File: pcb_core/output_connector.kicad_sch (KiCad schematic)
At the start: 5 parts, among them IC1 DRV8871DDA, J3 1053131103

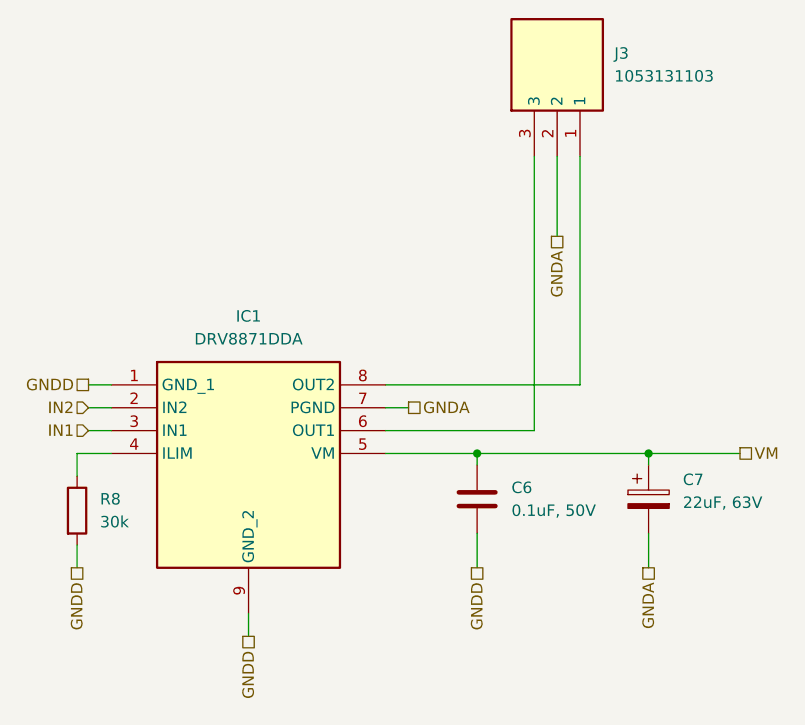
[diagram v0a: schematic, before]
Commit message: Correct BOM errors
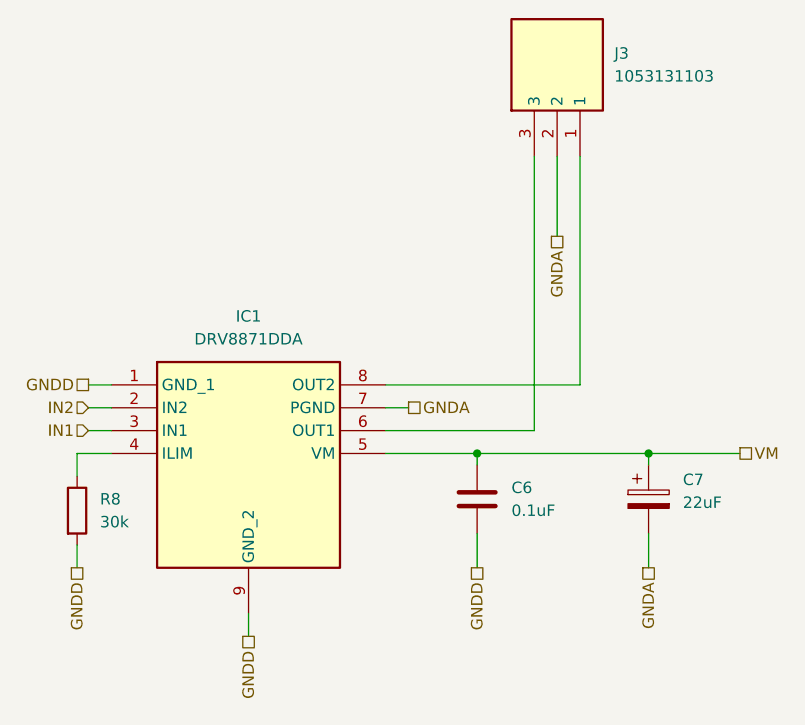
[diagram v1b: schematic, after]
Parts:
- C6: value 0.1uF, 50V -> 0.1uF
- C7: value 22uF, 63V -> 22uF
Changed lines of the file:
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@@
 			)
 		)
-		(property "Value" "0.1uF, 50V"
+		(property "Value" "0.1uF"
 			(at 128.27 111.7599 0)
 			(effects
@@
 			)
 		)
-		(property "Value" "22uF, 63V"
+		(property "Value" "22uF"
 			(at 147.32 110.8709 0)
 			(effects

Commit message: Correct ECR Warnings
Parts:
- IC1: Arrow Part Number (none) -> DRV8871DDA; Arrow Price/Stock (none) -> https://www.arrow.com/en/products/drv8871dda/texas-instrume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; Mouser Price/Stock (none) -> https://www.mouser.co.uk/ProductDetail/Texas-Instruments/DR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
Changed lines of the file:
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@@
 			)
 		)
-		(property "Description" ""
+		(property "Description" "Motor / Motion / Ignition Controllers & Drivers 3.6A Brushed DC Motor Driver with Integrated Current Sensing (PWM Ctrl) 8-SO PowerPAD -40 to 125"
 			(at 83.82 97.79 0)
 			(effects
@@
 				(hide yes)
 			)
+		)
+		(property "Mouser Price/Stock" "https://www.mouser.co.uk/ProductDetail/Texas-Instruments/DRV8871DDA?qs=Fobv33ltQGiluwfB07aSBw%3D%3D"
+			(at 110.49 892.71 0)
+			(effects
+				(font
+					(size 1.27 1.27)
+				)
+				(justify left top)
+				(hide yes)
+			)
+		)
+		(property "Arrow Part Number" "DRV8871DDA"
+			(at 110.49 992.71 0)
+			(effects
+				(font
+					(size 1.27 1.27)
+				)
+				(justify left top)
+				(hide yes)
+			)
+		)
+		(property "Arrow Price/Stock" "https://www.arrow.com/en/products/drv8871dda/texas-instruments?region=nac"
+			(at 110.49 1092.71 0)
+			(effects
+				(font
+					(size 1.27 1.27)
+				)
+				(justify left top)
+				(hide yes)
+			)

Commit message: Harmonize package sizing of components
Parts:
- C6: Manufacturer_Part_Number (none) -> Capacitor, 0.1uF, 50V, 0805 SMD
- C7: LCSC# C473196 -> C5246567; Manufacturer_Part_Number (none) -> Polarized Capacitor, 22.0uF, 63V, D6.3xL7.7 SMD
- R8: LCSC# C319666 -> C2907479
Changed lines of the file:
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@@
 			)
 		)
-		(property "Manufacturer_Part_Number" ""
+		(property "Manufacturer_Part_Number" "Capacitor, 0.1uF, 50V, 0805 SMD"
 			(at 124.46 110.49 0)
 			(effects
@@
 			)
 		)
-		(property "Manufacturer_Part_Number" ""
+		(property "Manufacturer_Part_Number" "Polarized Capacitor, 22.0uF, 63V, D6.3xL7.7 SMD"
 			(at 143.51 110.49 0)
 			(effects
@@
 			)
 		)
-		(property "LCSC#" "C473196"
+		(property "LCSC#" "C5246567"
 			(at 143.51 110.49 0)
 			(effects
@@
 			)
 		)
-		(property "LCSC#" "C319666"
+		(property "LCSC#" "C2907479"
 			(at 80.01 111.76 0)
 			(effects

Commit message: Add AISLER bom support and assigned components
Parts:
- C6: AISLER_MPN (none) -> 100.0nF, 0805 SMD
- IC1: AISLER_MPN (none) -> DRV8871DDA
- J3: AISLER_MPN (none) -> 1053131103
- R8: AISLER_MPN (none) -> 30.0kΩ, 1206 SMD
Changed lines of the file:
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@@
+			)
+		)
+		(property "AISLER_MPN" "100.0nF, 0805 SMD"
+			(at 124.46 110.49 0)
+			(effects
+				(font
+					(size 1.27 1.27)
+				)
+				(hide yes)
 			)
 		)
@@
 			)
 		)
+		(property "AISLER_MPN" ""
+			(at 143.51 110.49 0)
+			(effects
+				(font
+					(size 1.27 1.27)
+				)
+				(hide yes)
+			)
+		)
 		(pin "1"
 		)
@@
 			)
 		)
+		(property "AISLER_MPN" "DRV8871DDA"
+			(at 83.82 97.79 0)
+			(effects
+				(font
+					(size 1.27 1.27)
+				)
+				(hide yes)
+			)
+		)
 		(pin "9"
 		)
@@
 			)
 		)
+		(property "AISLER_MPN" "30.0kΩ, 1206 SMD "
+			(at 80.01 111.76 0)
+			(effects
+				(font
+					(size 1.27 1.27)
+				)
+				(hide yes)
+			)
+		)
 		(pin "1"
 		)
@@
 			(at 130.81 72.39 0)
 			(effects
+				(font
+					(size 1.27 1.27)
+				)
+				(hide yes)
+			)
+		)
+		(property "AISLER_MPN" "1053131103"
+			(at 130.81 72.39 0)
+			(effects

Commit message: Update BOM Mouser
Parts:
- C6: Mouser Part Number (none) -> 80-C0805C104M5R
- C7: Mouser Part Number (none) -> 710-865080745011
- R8: Mouser Part Number (none) -> 652-CR1206FX-3002ELF
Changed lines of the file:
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@@
+			)
+		)
+		(property "Mouser Part Number" " 80-C0805C104M5R "
+			(at 124.46 110.49 0)
+			(effects
+				(font
+					(size 1.27 1.27)
+				)
+				(hide yes)
+			)
+		)
+		(property "Mouser# Alt1" ""
+			(at 124.46 110.49 0)
+			(effects
+				(font
+					(size 1.27 1.27)
+				)
+				(hide yes)
 			)
 		)
@@
 			)
 		)
+		(property "Mouser Part Number" "710-865080745011"
+			(at 143.51 110.49 0)
+			(effects
+				(font
+					(size 1.27 1.27)
+				)
+				(hide yes)
+			)
+		)
+		(property "Mouser# Alt1" ""
+			(at 143.51 110.49 0)
+			(effects
+				(font
+					(size 1.27 1.27)
+				)
+				(hide yes)
+			)
+		)
 		(pin "1"
 		)
@@
 			)
 		)
+		(property "Mouser# Alt1" ""
+			(at 83.82 97.79 0)
+			(effects
+				(font
+					(size 1.27 1.27)
+				)
+				(hide yes)
+			)
+		)
 		(pin "9"
 		)
@@
 			)
 		)
+		(property "Mouser Part Number" "652-CR1206FX-3002ELF "
+			(at 80.01 111.76 0)
+			(effects
+				(font
+					(size 1.27 1.27)
+				)
+				(hide yes)
+			)
+		)
+		(property "Mouser# Alt1" ""
+			(at 80.01 111.76 0)
+			(effects
+				(font
+					(size 1.27 1.27)
+				)
+				(hide yes)
+			)
+		)
 		(pin "1"
 		)
@@
 			(at 130.81 72.39 0)
 			(effects
+				(font
+					(size 1.27 1.27)
+				)
+				(hide yes)
+			)
+		)
+		(property "Mouser# Alt1" ""
+			(at 130.81 72.39 0)
+			(effects
